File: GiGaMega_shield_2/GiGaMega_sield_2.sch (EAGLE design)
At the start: 34 parts

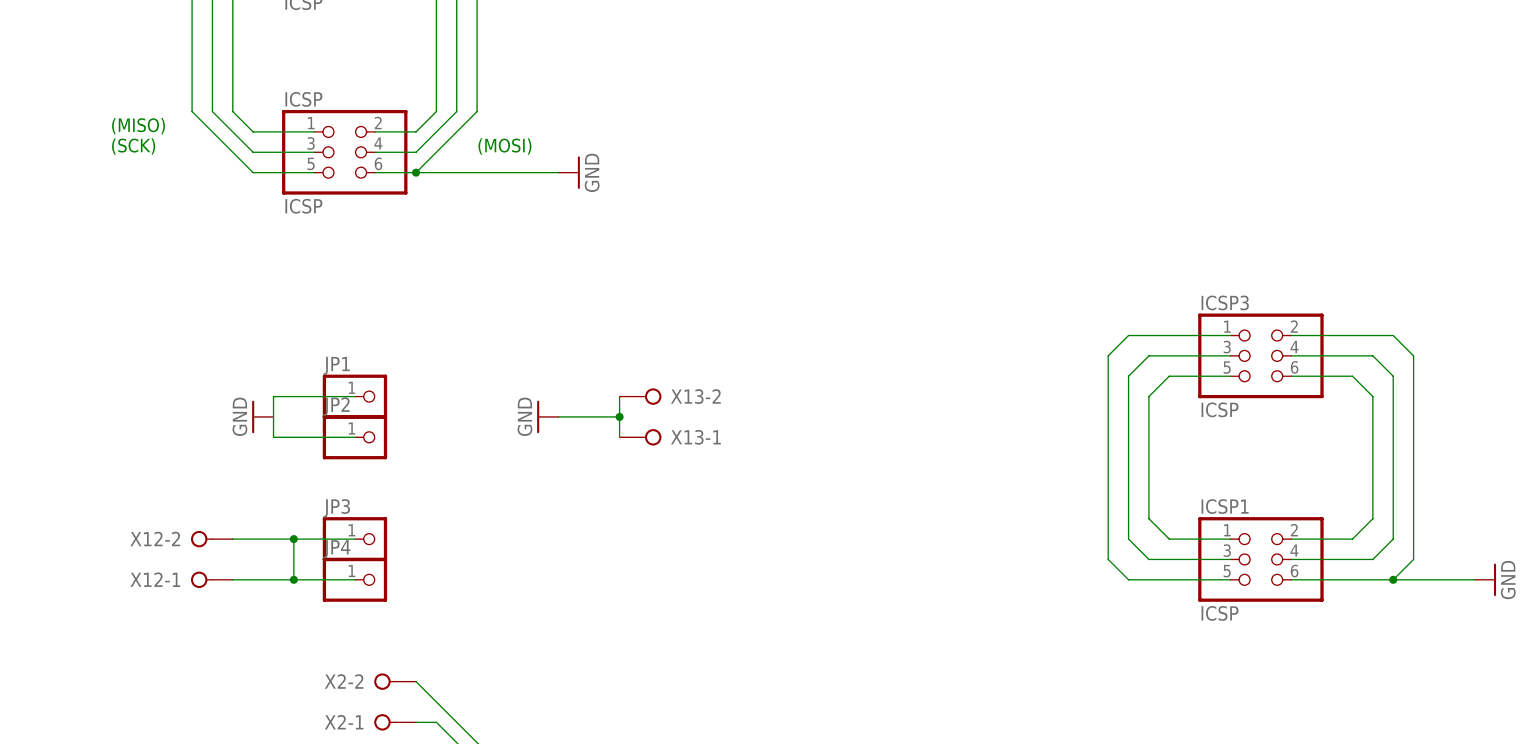
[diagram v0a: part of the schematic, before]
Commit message: Correct SPI connectors
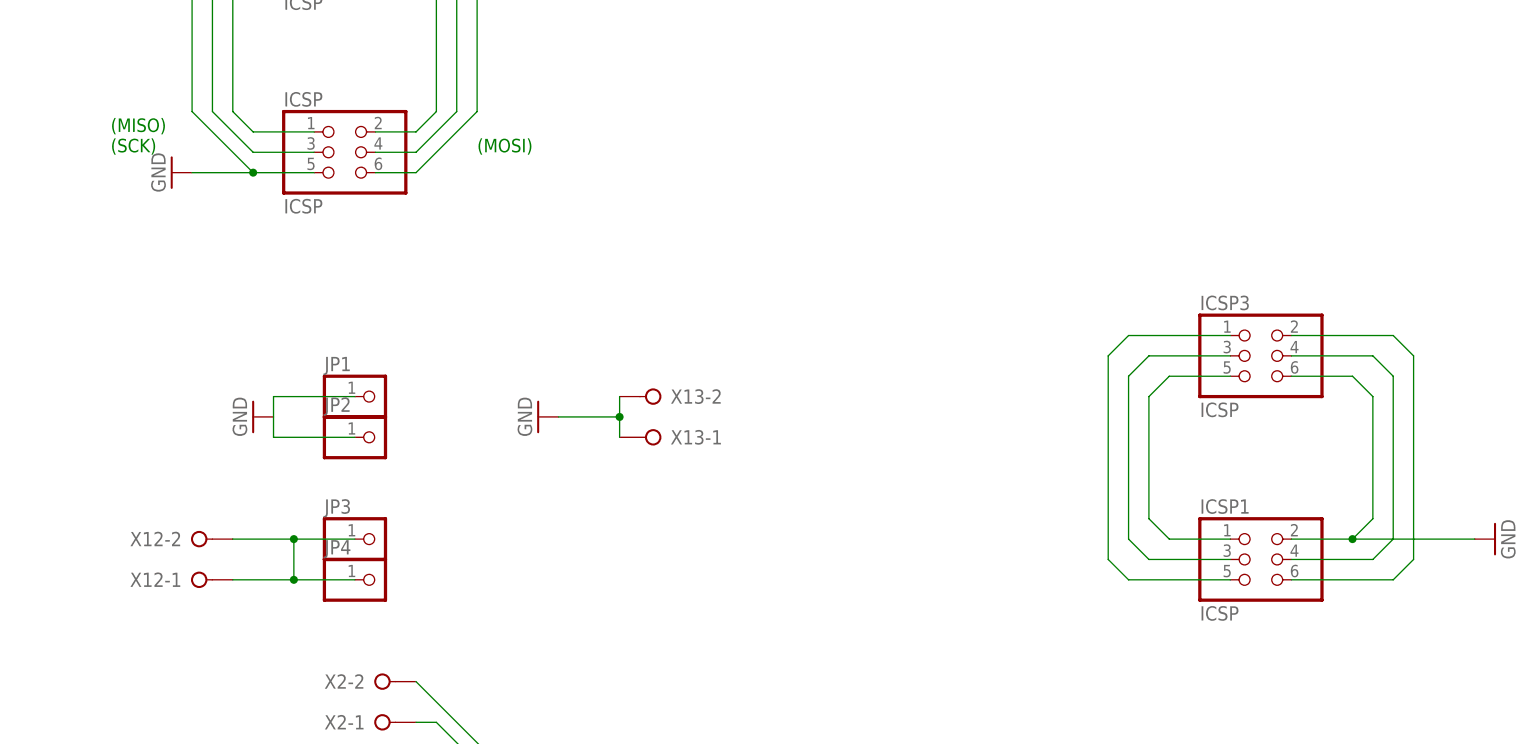
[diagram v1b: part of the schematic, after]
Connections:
- removed net N$17 (its old number): ICSP.5, ICSP2.1
- removed net N$22: ICSP1.2, ICSP3.6
- new net N$20: ICSP1.6, ICSP3.2
- new net N$21: ICSP.6, ICSP2.2
- net GND: now also ICSP.5, ICSP1.2, ICSP2.1, ICSP3.6; no longer ICSP.6, ICSP1.6, ICSP2.2, ICSP3.2
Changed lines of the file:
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@@
 <instance part="GND5" gate="1" x="71.12" y="93.98" rot="R90"/>
 <instance part="C1" gate="G$1" x="58.42" y="88.9"/>
-<instance part="GND6" gate="1" x="426.72" y="99.06" rot="R90"/>
-<instance part="GND7" gate="1" x="312.42" y="149.86" rot="R90"/>
+<instance part="GND6" gate="1" x="426.72" y="104.14" rot="R90"/>
+<instance part="GND7" gate="1" x="261.62" y="149.86" rot="R270"/>
 </instances>
 <busses>
@@
 </segment>
 <segment>
-<pinref part="ICSP2" gate="A" pin="2"/>
-<wire x1="287.02" y1="180.34" x2="292.1" y2="180.34" width="0.1524" layer="91"/>
-<wire x1="292.1" y1="180.34" x2="299.72" y2="172.72" width="0.1524" layer="91"/>
-<wire x1="299.72" y1="172.72" x2="299.72" y2="157.48" width="0.1524" layer="91"/>
-<wire x1="299.72" y1="157.48" x2="292.1" y2="149.86" width="0.1524" layer="91"/>
-<pinref part="ICSP" gate="A" pin="6"/>
-<wire x1="292.1" y1="149.86" x2="287.02" y2="149.86" width="0.1524" layer="91"/>
+<pinref part="ICSP2" gate="A" pin="1"/>
+<wire x1="279.4" y1="180.34" x2="271.78" y2="180.34" width="0.1524" layer="91"/>
+<wire x1="271.78" y1="180.34" x2="264.16" y2="172.72" width="0.1524" layer="91"/>
+<wire x1="264.16" y1="172.72" x2="264.16" y2="157.48" width="0.1524" layer="91"/>
+<wire x1="264.16" y1="157.48" x2="271.78" y2="149.86" width="0.1524" layer="91"/>
+<pinref part="ICSP" gate="A" pin="5"/>
+<wire x1="271.78" y1="149.86" x2="279.4" y2="149.86" width="0.1524" layer="91"/>
 <pinref part="GND7" gate="1" pin="GND"/>
-<wire x1="309.88" y1="149.86" x2="292.1" y2="149.86" width="0.1524" layer="91"/>
-<junction x="292.1" y="149.86"/>
-</segment>
-<segment>
-<pinref part="ICSP1" gate="A" pin="6"/>
-<wire x1="401.32" y1="99.06" x2="414.02" y2="99.06" width="0.1524" layer="91"/>
-<wire x1="414.02" y1="99.06" x2="416.56" y2="101.6" width="0.1524" layer="91"/>
-<wire x1="416.56" y1="101.6" x2="416.56" y2="127" width="0.1524" layer="91"/>
-<wire x1="416.56" y1="127" x2="414.02" y2="129.54" width="0.1524" layer="91"/>
-<pinref part="ICSP3" gate="A" pin="2"/>
-<wire x1="414.02" y1="129.54" x2="401.32" y2="129.54" width="0.1524" layer="91"/>
+<wire x1="264.16" y1="149.86" x2="271.78" y2="149.86" width="0.1524" layer="91"/>
+<junction x="271.78" y="149.86"/>
+</segment>
+<segment>
+<pinref part="ICSP3" gate="A" pin="6"/>
+<wire x1="401.32" y1="124.46" x2="408.94" y2="124.46" width="0.1524" layer="91"/>
+<wire x1="408.94" y1="124.46" x2="411.48" y2="121.92" width="0.1524" layer="91"/>
+<wire x1="411.48" y1="121.92" x2="411.48" y2="106.68" width="0.1524" layer="91"/>
+<wire x1="411.48" y1="106.68" x2="408.94" y2="104.14" width="0.1524" layer="91"/>
+<pinref part="ICSP1" gate="A" pin="2"/>
+<wire x1="408.94" y1="104.14" x2="401.32" y2="104.14" width="0.1524" layer="91"/>
 <pinref part="GND6" gate="1" pin="GND"/>
-<wire x1="424.18" y1="99.06" x2="414.02" y2="99.06" width="0.1524" layer="91"/>
-<junction x="414.02" y="99.06"/>
+<wire x1="424.18" y1="104.14" x2="408.94" y2="104.14" width="0.1524" layer="91"/>
+<junction x="408.94" y="104.14"/>
 </segment>
 </net>
@@
 </segment>
 </net>
-<net name="N$17" class="0">
-<segment>
-<pinref part="ICSP2" gate="A" pin="1"/>
-<wire x1="279.4" y1="180.34" x2="271.78" y2="180.34" width="0.1524" layer="91"/>
-<wire x1="271.78" y1="180.34" x2="264.16" y2="172.72" width="0.1524" layer="91"/>
-<wire x1="264.16" y1="172.72" x2="264.16" y2="157.48" width="0.1524" layer="91"/>
-<wire x1="264.16" y1="157.48" x2="271.78" y2="149.86" width="0.1524" layer="91"/>
-<pinref part="ICSP" gate="A" pin="5"/>
-<wire x1="271.78" y1="149.86" x2="279.4" y2="149.86" width="0.1524" layer="91"/>
-</segment>
-</net>
 <net name="N$18" class="0">
 <segment>
@@
 <pinref part="ICSP3" gate="A" pin="3"/>
 <wire x1="383.54" y1="127" x2="393.7" y2="127" width="0.1524" layer="91"/>
-</segment>
-</net>
-<net name="N$21" class="0">
-<segment>
-<pinref part="ICSP1" gate="A" pin="5"/>
-<wire x1="393.7" y1="99.06" x2="381" y2="99.06" width="0.1524" layer="91"/>
-<wire x1="381" y1="99.06" x2="378.46" y2="101.6" width="0.1524" layer="91"/>
-<wire x1="378.46" y1="101.6" x2="378.46" y2="127" width="0.1524" layer="91"/>
-<wire x1="378.46" y1="127" x2="381" y2="129.54" width="0.1524" layer="91"/>
-<pinref part="ICSP3" gate="A" pin="1"/>
-<wire x1="381" y1="129.54" x2="393.7" y2="129.54" width="0.1524" layer="91"/>
-</segment>
-</net>
-<net name="N$22" class="0">
-<segment>
-<pinref part="ICSP3" gate="A" pin="6"/>
-<wire x1="401.32" y1="124.46" x2="408.94" y2="124.46" width="0.1524" layer="91"/>
-<wire x1="408.94" y1="124.46" x2="411.48" y2="121.92" width="0.1524" layer="91"/>
-<wire x1="411.48" y1="121.92" x2="411.48" y2="106.68" width="0.1524" layer="91"/>
-<wire x1="411.48" y1="106.68" x2="408.94" y2="104.14" width="0.1524" layer="91"/>
-<pinref part="ICSP1" gate="A" pin="2"/>
-<wire x1="408.94" y1="104.14" x2="401.32" y2="104.14" width="0.1524" layer="91"/>
 </segment>
 </net>
@@
 </segment>
 </net>
+<net name="N$20" class="0">
+<segment>
+<wire x1="414.02" y1="99.06" x2="416.56" y2="101.6" width="0.1524" layer="91"/>
+<wire x1="416.56" y1="101.6" x2="416.56" y2="127" width="0.1524" layer="91"/>
+<wire x1="416.56" y1="127" x2="414.02" y2="129.54" width="0.1524" layer="91"/>
+<pinref part="ICSP3" gate="A" pin="2"/>
+<wire x1="414.02" y1="129.54" x2="401.32" y2="129.54" width="0.1524" layer="91"/>
+<pinref part="ICSP1" gate="A" pin="6"/>
+<wire x1="414.02" y1="99.06" x2="401.32" y2="99.06" width="0.1524" layer="91"/>
+</segment>
+</net>
+<net name="N$21" class="0">
+<segment>
+<pinref part="ICSP2" gate="A" pin="2"/>
+<wire x1="287.02" y1="180.34" x2="292.1" y2="180.34" width="0.1524" layer="91"/>
+<wire x1="292.1" y1="180.34" x2="299.72" y2="172.72" width="0.1524" layer="91"/>
+<wire x1="299.72" y1="172.72" x2="299.72" y2="157.48" width="0.1524" layer="91"/>
+<wire x1="299.72" y1="157.48" x2="292.1" y2="149.86" width="0.1524" layer="91"/>
+<pinref part="ICSP" gate="A" pin="6"/>
+<wire x1="292.1" y1="149.86" x2="287.02" y2="149.86" width="0.1524" layer="91"/>
+</segment>
+</net>
+<net name="N$17" class="0">
+<segment>
+<pinref part="ICSP3" gate="A" pin="1"/>
+<pinref part="ICSP1" gate="A" pin="5"/>
+<wire x1="393.7" y1="99.06" x2="381" y2="99.06" width="0.1524" layer="91"/>
+<wire x1="381" y1="99.06" x2="378.46" y2="101.6" width="0.1524" layer="91"/>
+<wire x1="378.46" y1="101.6" x2="378.46" y2="127" width="0.1524" layer="91"/>
+<wire x1="378.46" y1="127" x2="381" y2="129.54" width="0.1524" layer="91"/>
+<wire x1="381" y1="129.54" x2="393.7" y2="129.54" width="0.1524" layer="91"/>
+</segment>
+</net>
